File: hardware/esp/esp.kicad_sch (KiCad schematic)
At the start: 40 parts, among them J1 Conn_01x02, J2 USB_C_Receptacle_USB2.0_16P, J3 USB_C_Receptacle_USB2.0_16P, J4 Conn_01x02, SW1 RESET, SW2 BOOT, U1 AMS1117-3.3, U2 CP2102N-Axx-xQFN20, U3 ESP32-S3-WROOM-1

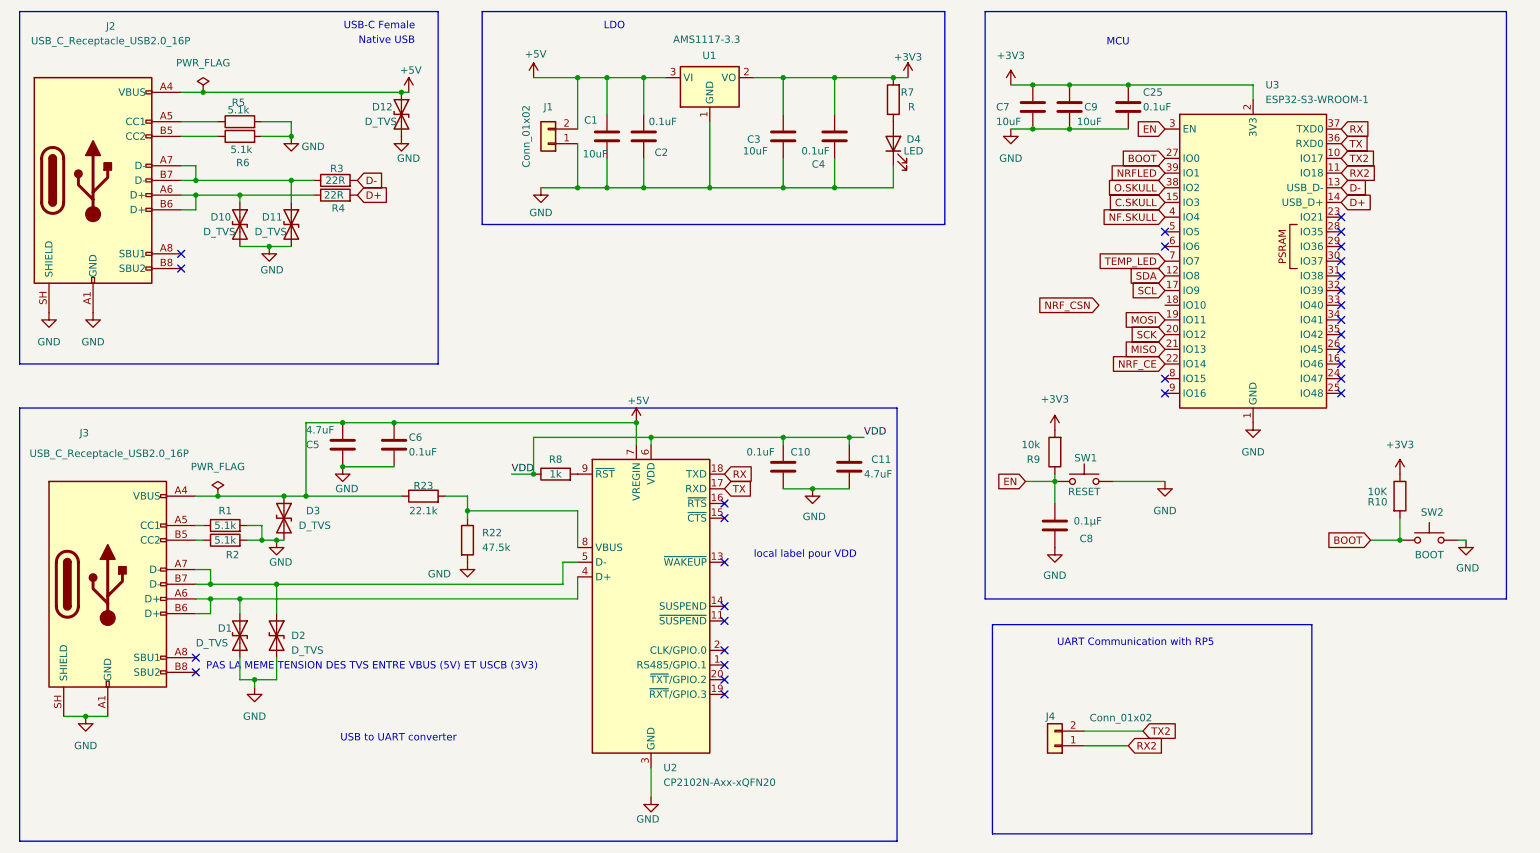
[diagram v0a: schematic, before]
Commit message: Updating BOM, adding fixes to the PCB and silkscreen finishes
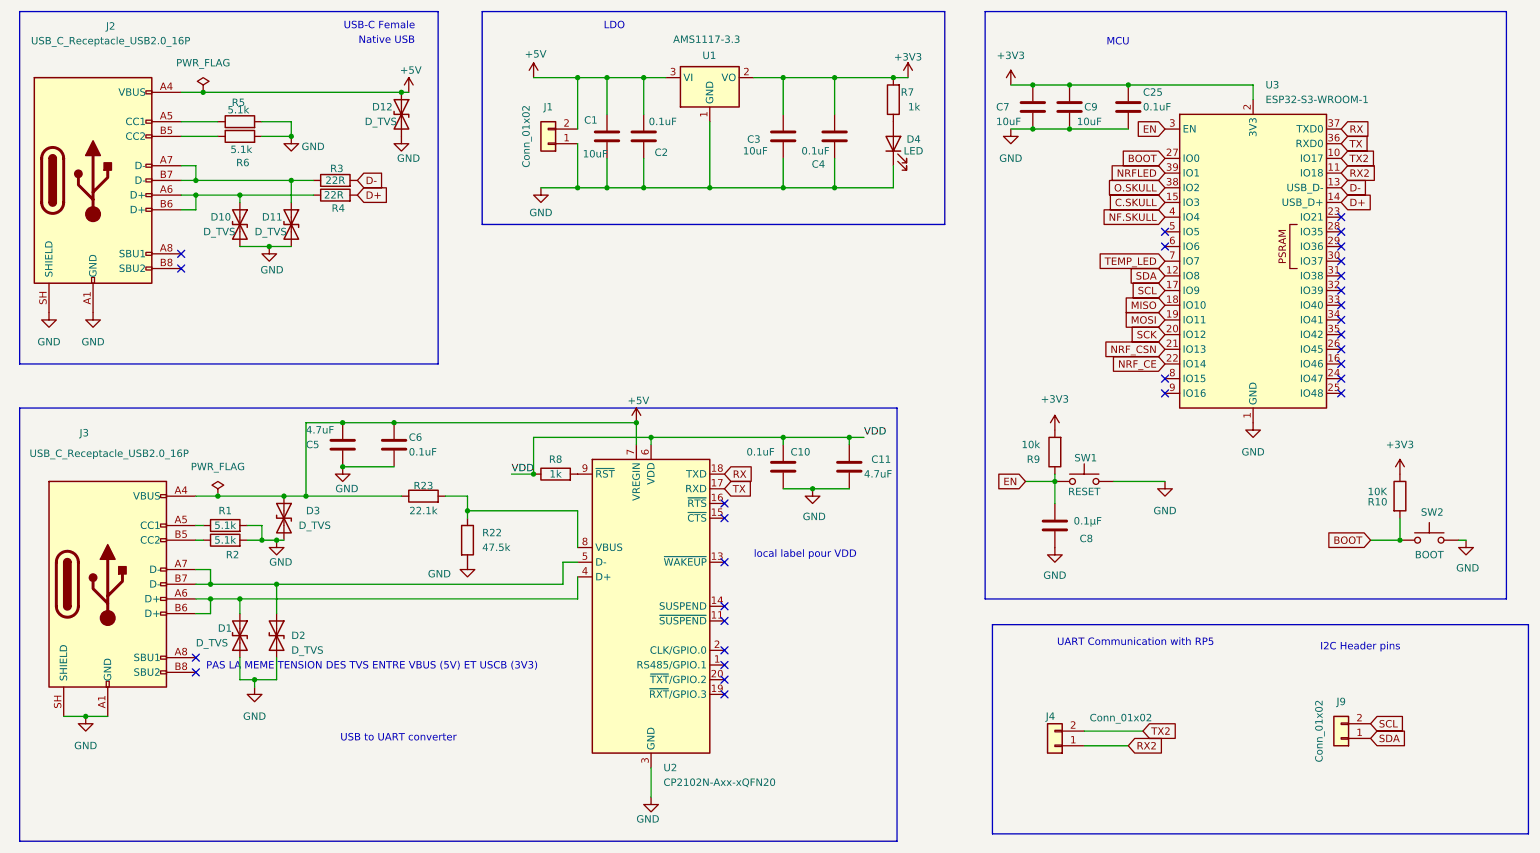
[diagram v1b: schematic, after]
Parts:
- added J9: Conn_01x02, Connector_PinHeader_2.54mm:PinHeader_1x02_P2.54mm_Vertical, symbol Connector_Generic:Conn_01x02
- R7: value R -> 1k
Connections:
- net MISO: now also U3.18 (IO10); no longer U3.21 (IO13)
- net NRF_CSN: now also U3.21 (IO13)
- net SCL: now also J9.2 (Pin_2)
- net SDA: now also J9.1 (Pin_1)
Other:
- note added: "I2C Header pins"
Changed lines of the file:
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@@
 	(rectangle
 		(start 187.325 121.285)
-		(end 242.57 157.48)
+		(end 280.035 157.48)
 		(stroke
 			(width 0)
@@
 		)
 	)
+	(text "I2C Header pins"
+		(exclude_from_sim no)
+		(at 250.952 125.222 0)
+		(effects
+			(font
+				(size 1.27 1.27)
+			)
+		)
+	)
 	(text "USB to UART converter"
 		(exclude_from_sim no)
@@
 		)
 	)
+	(global_label "SCL"
+		(shape input)
+		(at 252.73 138.43 0)
+		(fields_autoplaced yes)
+		(effects
+			(font
+				(size 1.27 1.27)
+			)
+			(justify left)
+		)
+		(property "Intersheetrefs" "${INTERSHEET_REFS}"
+			(at 259.2228 138.43 0)
+			(hide yes)
+			(show_name no)
+			(do_not_autoplace no)
+			(effects
+				(font
+					(size 1.27 1.27)
+				)
+				(justify left)
+			)
+		)
+	)
 	(global_label "TX"
 		(shape input)
@@
 		)
 	)
+	(global_label "SDA"
+		(shape input)
+		(at 252.73 140.97 0)
+		(fields_autoplaced yes)
+		(effects
+			(font
+				(size 1.27 1.27)
+			)
+			(justify left)
+		)
+		(property "Intersheetrefs" "${INTERSHEET_REFS}"
+			(at 259.2833 140.97 0)
+			(hide yes)
+			(show_name no)
+			(do_not_autoplace no)
+			(effects
+				(font
+					(size 1.27 1.27)
+				)
+				(justify left)
+			)
+		)
+	)
 	(global_label "BOOT"
 		(shape input)
@@
 	(global_label "MISO"
 		(shape input)
-		(at 217.17 73.66 180)
+		(at 217.17 66.04 180)
 		(fields_autoplaced yes)
 		(effects
@@
 		)
 		(property "Intersheetrefs" "${INTERSHEET_REFS}"
-			(at 209.5886 73.66 0)
+			(at 209.5886 66.04 0)
 			(hide yes)
 			(show_name no)
@@
 	(global_label "NRF_CSN"
 		(shape input)
-		(at 205.74 66.04 180)
+		(at 217.17 73.66 180)
 		(fields_autoplaced yes)
 		(effects
@@
 		)
 		(property "Intersheetrefs" "${INTERSHEET_REFS}"
-			(at 193.5019 66.04 0)
+			(at 204.9319 73.66 0)
 			(hide yes)
 			(show_name no)
@@
 	)
 	(symbol
+		(lib_id "Connector_Generic:Conn_01x02")
+		(at 247.65 140.97 180)
+		(unit 1)
+		(body_style 1)
+		(exclude_from_sim no)
+		(in_bom yes)
+		(on_board yes)
+		(in_pos_files yes)
+		(dnp no)
+		(property "Reference" "J9"
+			(at 247.65 134.62 0)
+			(show_name no)
+			(do_not_autoplace no)
+			(effects
+				(font
+					(size 1.27 1.27)
+				)
+			)
+		)
+		(property "Value" "Conn_01x02"
+			(at 243.84 139.7 90)
+			(show_name no)
+			(do_not_autoplace no)
+			(effects
+				(font
+					(size 1.27 1.27)
+				)
+			)
+		)
+		(property "Footprint" "Connector_PinHeader_2.54mm:PinHeader_1x02_P2.54mm_Vertical"
+			(at 247.65 140.97 0)
+			(hide yes)
+			(show_name no)
+			(do_not_autoplace no)
+			(effects
+				(font
+					(size 1.27 1.27)
+				)
+			)
+		)
+		(property "Datasheet" ""
+			(at 247.65 140.97 0)
+			(hide yes)
+			(show_name no)
+			(do_not_autoplace no)
+			(effects
+				(font
+					(size 1.27 1.27)
+				)
+			)
+		)
+		(property "Description" "Generic connector, single row, 01x02, script generated (kicad-library-utils/schlib/autogen/connector/)"
+			(at 247.65 140.97 0)
+			(hide yes)
+			(show_name no)
+			(do_not_autoplace no)
+			(effects
+				(font
+					(size 1.27 1.27)
+				)
+			)
+		)
+		(property "Sim.Device" ""
+			(at 247.65 140.97 0)
+			(hide yes)
+			(show_name no)
+			(do_not_autoplace no)
+			(effects
+				(font
+					(size 1.27 1.27)
+				)
+			)
+		)
+		(property "Sim.Type" ""
+			(at 247.65 140.97 0)
+			(hide yes)
+			(show_name no)
+			(do_not_autoplace no)
+			(effects
+				(font
+					(size 1.27 1.27)
+				)
+			)
+		)
+		(pin "2"
+		)
+		(pin "1"
+		)
+		(instances
+			(project "esp"
+				(path "/1af9f8de-01c4-4db4-9e1a-5a2acf839c86"
+					(reference "J9")
+					(unit 1)
+				)
+			)
+		)
+	)
+	(symbol
 		(lib_id "power:GND")
 		(at 269.24 106.68 0)
@@
 			)
 		)
-		(property "Value" "R"
+		(property "Value" "1k"
 			(at 172.72 31.7499 0)
 			(show_name no)
